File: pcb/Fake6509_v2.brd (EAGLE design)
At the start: 70.5 x 20.3 mm, 14 parts, among them IC1 6509, IC2 65C02, IC4 XC9572XL

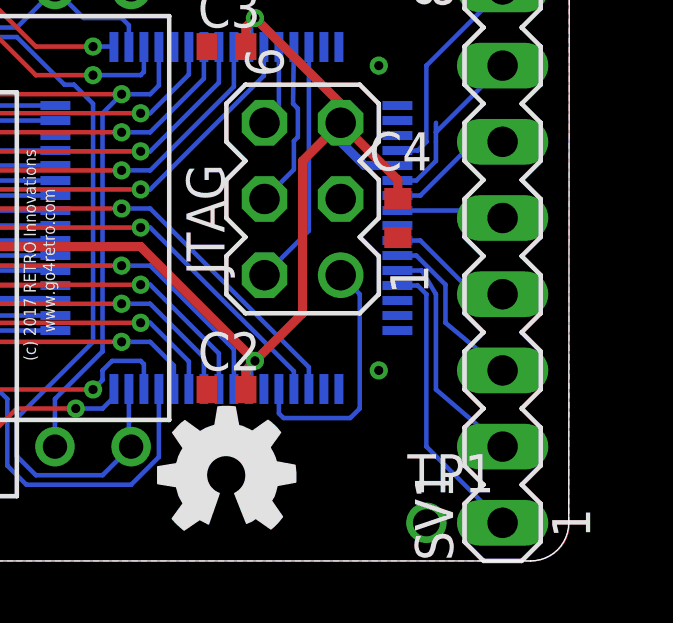
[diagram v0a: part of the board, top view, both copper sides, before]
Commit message: Added comments to Verilog and cleaned up a small bug in the PCB
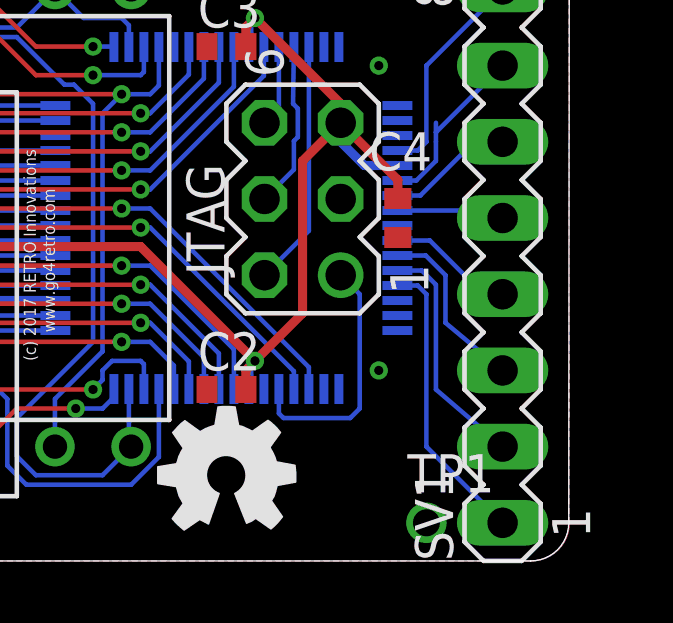
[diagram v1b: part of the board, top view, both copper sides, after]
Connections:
- net N$3 renamed PHI0_6502
- net PHI0 renamed PHI2_6509
- net PHI1 renamed PHI1_6509
- net PHI2 renamed PHI2_6502
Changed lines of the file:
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@@
 <wire x1="7.87" y1="11.18" x2="7.37" y2="11.68" width="0.1524" layer="16"/>
 </signal>
-<signal name="PHI2">
+<signal name="PHI2_6502">
 <contactref element="IC2" pad="39"/>
 </signal>
-<signal name="PHI0">
+<signal name="PHI2_6509">
 <contactref element="IC1" pad="40"/>
 <contactref element="SJ1" pad="3"/>
@@
 <wire x1="12.7" y1="8.89" x2="17.78" y2="3.81" width="0.1524" layer="1"/>
 </signal>
-<signal name="PHI1">
+<signal name="PHI1_6509">
 <contactref element="IC1" pad="38"/>
 <contactref element="SJ1" pad="1"/>
@@
 <wire x1="11.684" y1="13.97" x2="11.684" y2="15.24" width="0.1524" layer="1"/>
 </signal>
-<signal name="N$3">
+<signal name="PHI0_6502">
 <contactref element="SJ1" pad="2"/>
 <contactref element="IC2" pad="37"/>
@@
 <contactref element="SV1" pad="4"/>
 <contactref element="IC4" pad="42"/>
-<wire x1="64.755" y1="10.68" x2="65.52" y2="10.68" width="0.1524" layer="16"/>
-<wire x1="65.52" y1="10.68" x2="67.31" y2="8.89" width="0.1524" layer="16"/>
-<wire x1="67.31" y1="8.89" x2="68.2625" y2="8.89" width="0.1524" layer="16"/>
+<wire x1="64.755" y1="10.68" x2="65.8375" y2="10.68" width="0.1524" layer="16"/>
+<wire x1="65.8375" y1="10.68" x2="67.6275" y2="8.89" width="0.1524" layer="16"/>
+<wire x1="67.6275" y1="8.89" x2="68.2625" y2="8.89" width="0.1524" layer="16"/>
 </signal>
 <signal name="N$4">
 <contactref element="SV1" pad="3"/>
 <contactref element="IC4" pad="43"/>
-<wire x1="64.755" y1="10.18" x2="65.385" y2="10.18" width="0.1524" layer="16"/>
-<wire x1="65.385" y1="10.18" x2="66.3575" y2="9.2075" width="0.1524" layer="16"/>
-<wire x1="66.3575" y1="9.2075" x2="66.3575" y2="7.9375" width="0.1524" layer="16"/>
+<wire x1="64.755" y1="10.18" x2="65.7025" y2="10.18" width="0.1524" layer="16"/>
+<wire x1="65.7025" y1="10.18" x2="66.3575" y2="9.525" width="0.1524" layer="16"/>
+<wire x1="66.3575" y1="9.525" x2="66.3575" y2="7.9375" width="0.1524" layer="16"/>
 <wire x1="66.3575" y1="7.9375" x2="68.2625" y2="6.35" width="0.1524" layer="16"/>
 </signal>
@@
 <contactref element="IC4" pad="44"/>
 <wire x1="64.755" y1="9.68" x2="65.5675" y2="9.68" width="0.1524" layer="16"/>
-<wire x1="65.5675" y1="9.68" x2="66.04" y2="8.89" width="0.1524" layer="16"/>
-<wire x1="66.04" y1="8.89" x2="66.04" y2="5.715" width="0.1524" layer="16"/>
+<wire x1="65.5675" y1="9.68" x2="66.04" y2="9.2075" width="0.1524" layer="16"/>
+<wire x1="66.04" y1="9.2075" x2="66.04" y2="5.715" width="0.1524" layer="16"/>
 <wire x1="66.04" y1="5.715" x2="68.2625" y2="3.81" width="0.1524" layer="16"/>
 </signal>

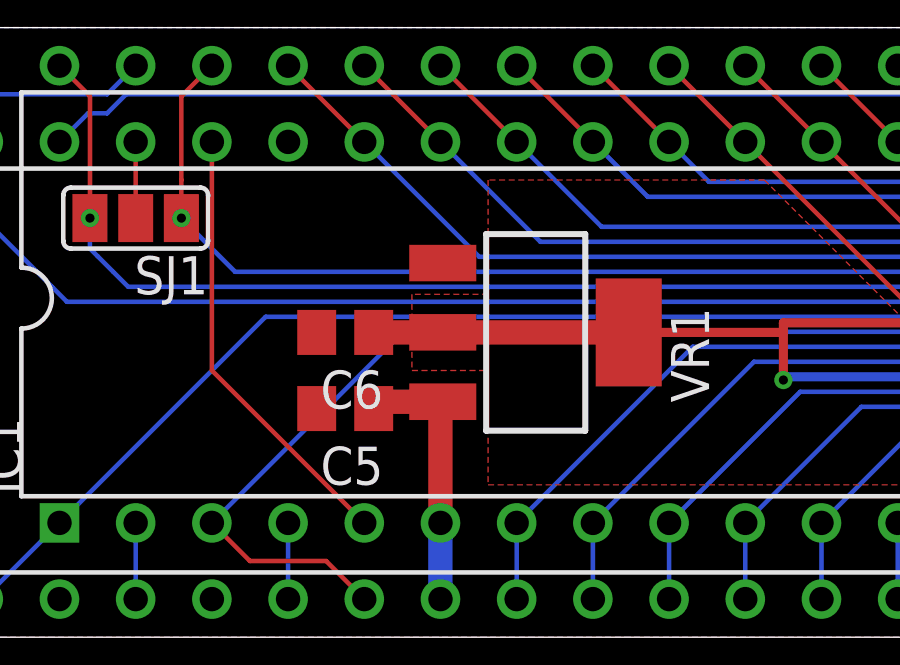
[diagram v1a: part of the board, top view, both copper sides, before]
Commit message: More changes to Verilog and PCB cleanup
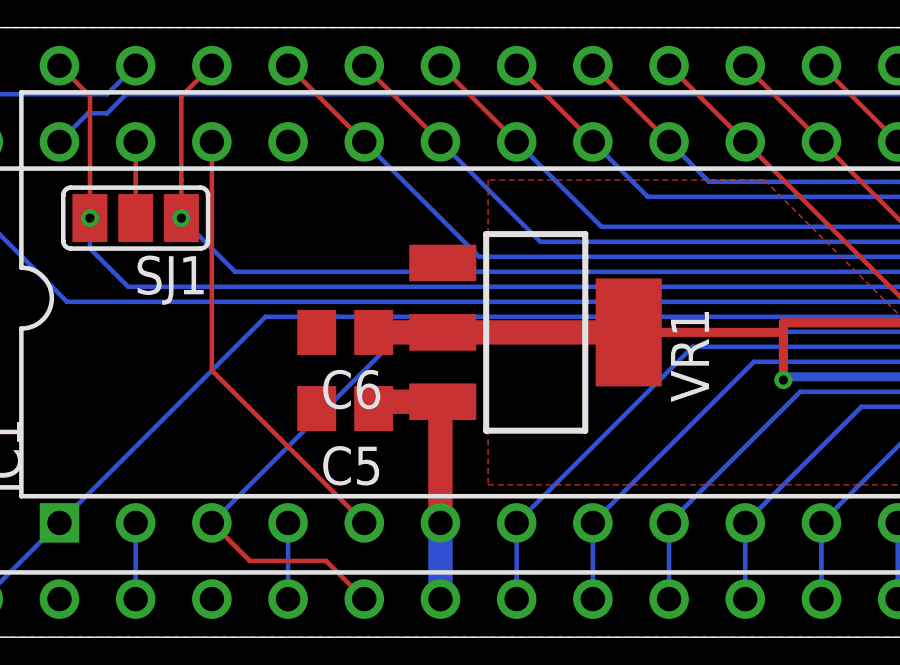
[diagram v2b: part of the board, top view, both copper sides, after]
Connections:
- net PHI0_6502 renamed PHI2I_6502
- net PHI1_6509 renamed PHI1I_6509
- net PHI2_6502 renamed PHI2O_6502
- net PHI2_6509 renamed PHI2I_6509
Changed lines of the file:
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@@
 <wire x1="7.87" y1="11.18" x2="7.37" y2="11.68" width="0.1524" layer="16"/>
 </signal>
-<signal name="PHI2_6502">
+<signal name="PHI2O_6502">
 <contactref element="IC2" pad="39"/>
 </signal>
-<signal name="PHI2_6509">
+<signal name="PHI2I_6509">
 <contactref element="IC1" pad="40"/>
 <contactref element="SJ1" pad="3"/>
@@
 <polygon width="0.3048" layer="1">
 <vertex x="21.9075" y="15.24"/>
-<vertex x="21.9075" y="11.43"/>
-<vertex x="19.3675" y="11.43"/>
-<vertex x="19.3675" y="8.89"/>
-<vertex x="21.9075" y="8.89"/>
 <vertex x="21.9075" y="5.08"/>
 <vertex x="36.5125" y="5.08"/>
@@
 <wire x1="12.7" y1="8.89" x2="17.78" y2="3.81" width="0.1524" layer="1"/>
 </signal>
-<signal name="PHI1_6509">
+<signal name="PHI1I_6509">
 <contactref element="IC1" pad="38"/>
 <contactref element="SJ1" pad="1"/>
@@
 <wire x1="11.684" y1="13.97" x2="11.684" y2="15.24" width="0.1524" layer="1"/>
 </signal>
-<signal name="PHI0_6502">
+<signal name="PHI2I_6502">
 <contactref element="SJ1" pad="2"/>
 <contactref element="IC2" pad="37"/>
